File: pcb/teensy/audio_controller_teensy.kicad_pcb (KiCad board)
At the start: 2 copper layers, 69.8 x 40.6 mm, 15 parts, among them P1 HEADER_02X08_SMD, SW1 SPST_SLIDE_AS, U1 TLE7230R

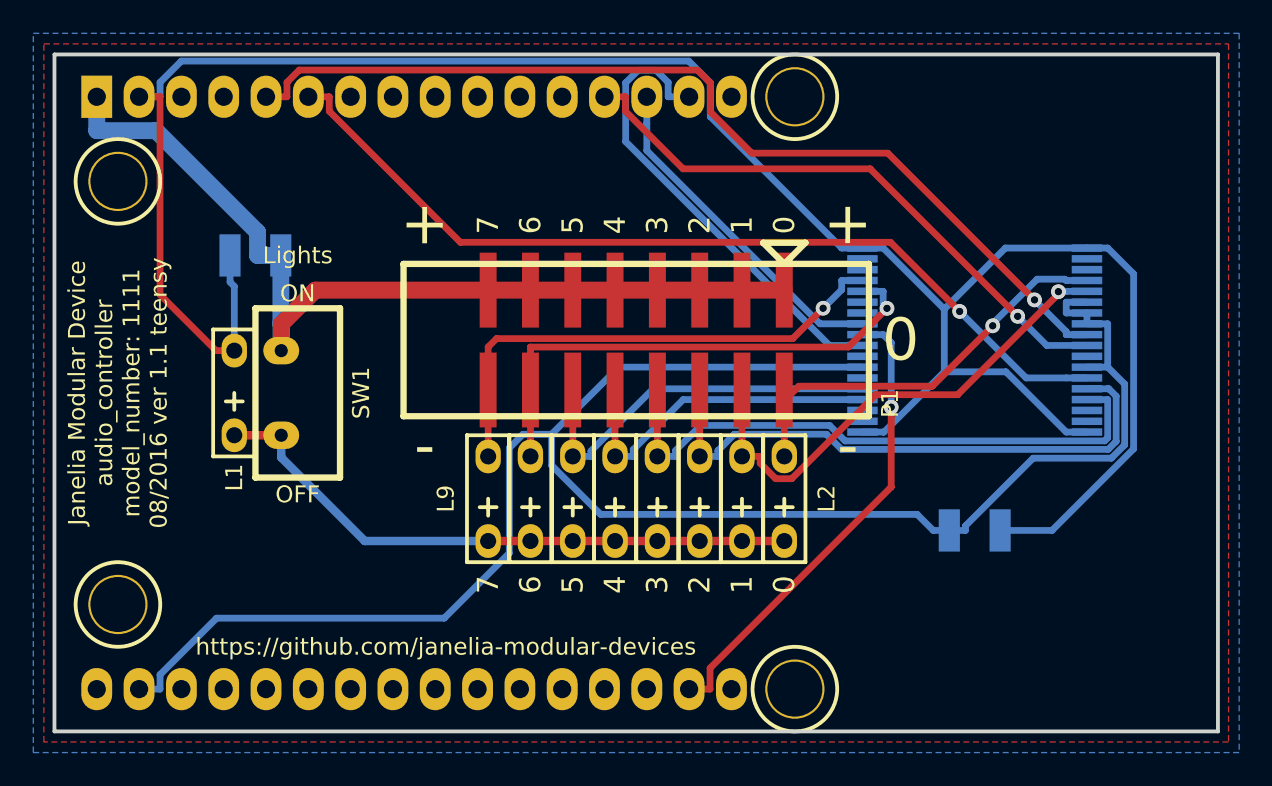
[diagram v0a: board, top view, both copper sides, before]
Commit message: Preparation for schematic editing.
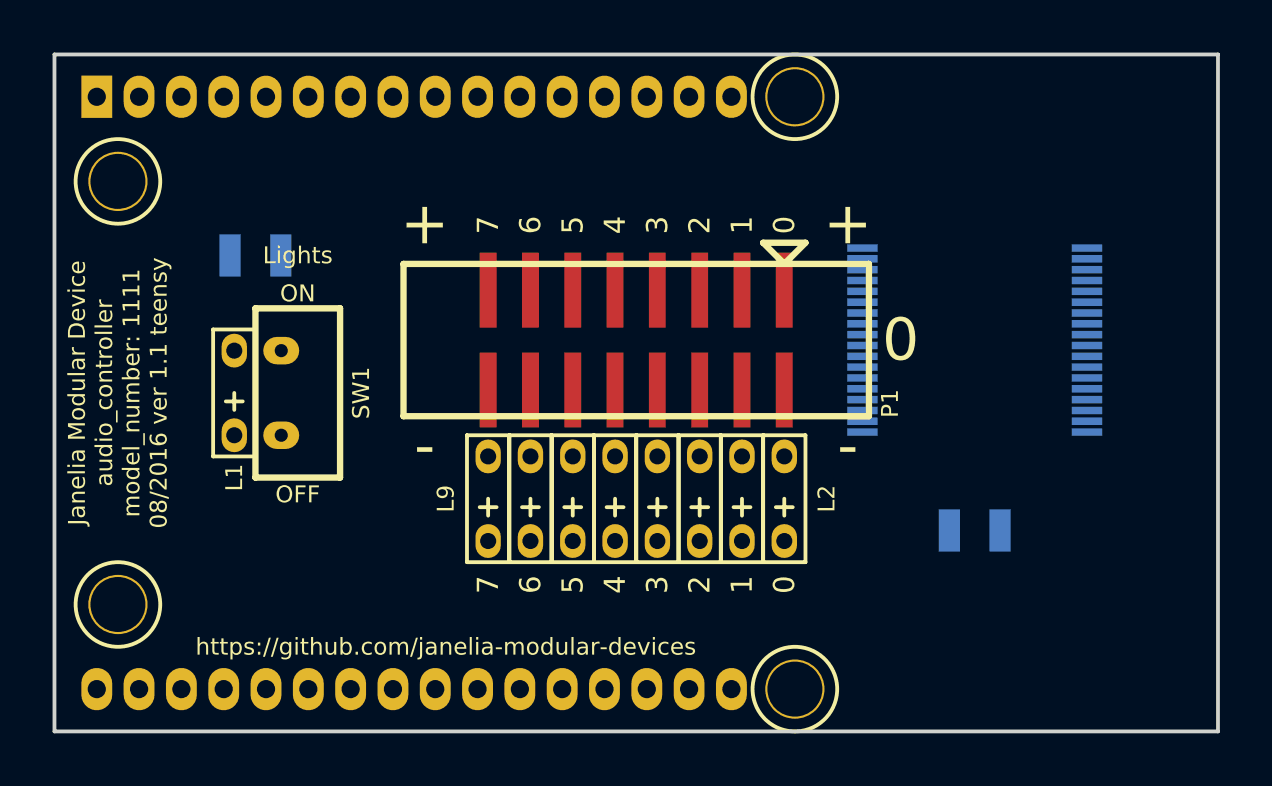
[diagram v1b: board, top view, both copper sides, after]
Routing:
- net GND: track 136.2 -> 0.00 mm
- net VEE: track 109.8 -> 0.00 mm
- net /RESET: track 58.2 -> 0.00 mm, vias 1 -> 0
- net VDD: track 55.4 -> 0.00 mm
- net /PWM: track 54.2 -> 0.00 mm, vias 1 -> 0
- net /LED_PWR: track 36.4 -> 0.00 mm
- net /OUT3: track 36.0 -> 0.00 mm
- net /CS: track 35.7 -> 0.00 mm, vias 1 -> 0
- net /OUT2: track 35.0 -> 0.00 mm
- net /OUT6: track 31.3 -> 0.00 mm, vias 1 -> 0
- net /OUT7: track 31.0 -> 0.00 mm, vias 1 -> 0
- net /OUT1: track 30.2 -> 0.00 mm, vias 1 -> 0
- net /SCK: track 28.5 -> 0.00 mm, vias 1 -> 0
- net /MISO: track 28.1 -> 0.00 mm
- net /OUT0: track 25.3 -> 0.00 mm, vias 1 -> 0
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- removed copper zone on B.Cu, net GND
- removed copper zone on F.Cu, net VDD
